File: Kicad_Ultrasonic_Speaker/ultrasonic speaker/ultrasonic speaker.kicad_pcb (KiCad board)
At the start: 2 copper layers, 99.1 x 86.4 mm, 12 parts, among them J1 To_Array, J2 Conn_01x02_Female, U1 ESP32_DevKit_V1_DOIT, U2 MIC4427, U3 LM317

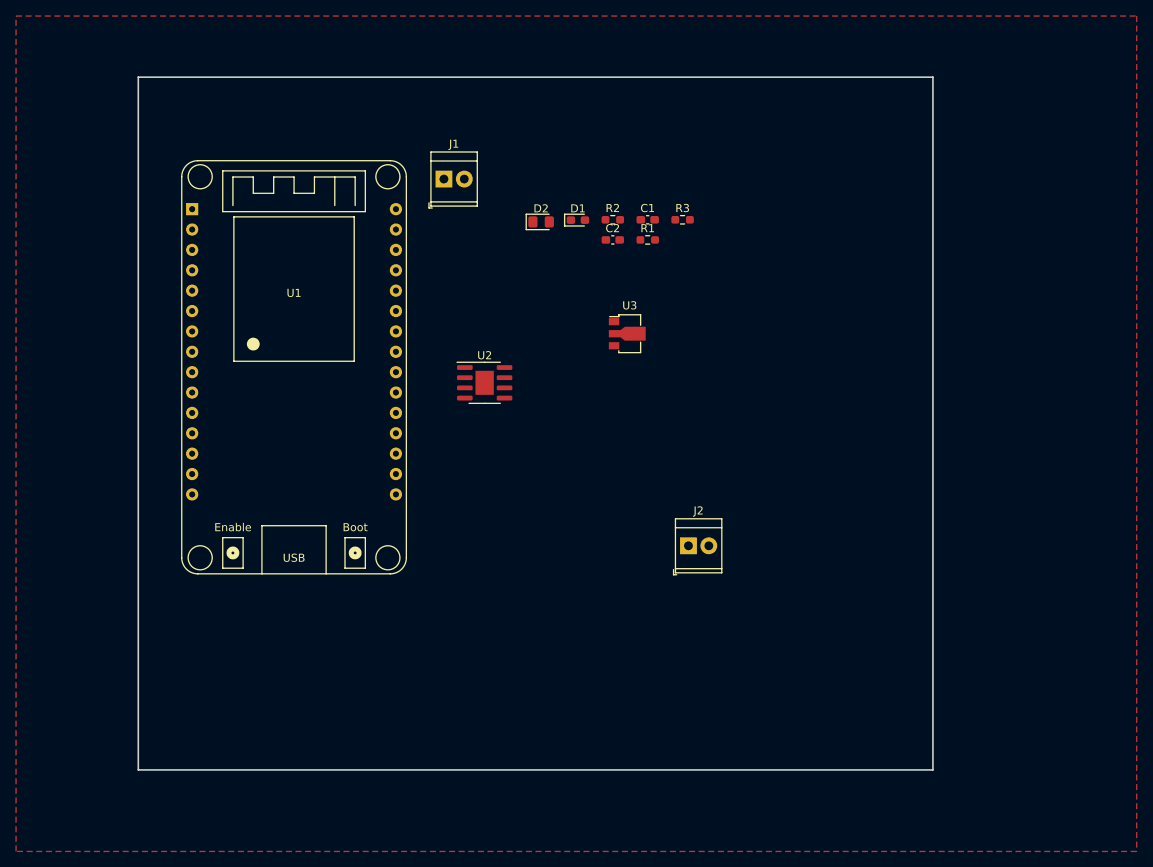
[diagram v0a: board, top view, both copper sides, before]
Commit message: change for boost converter
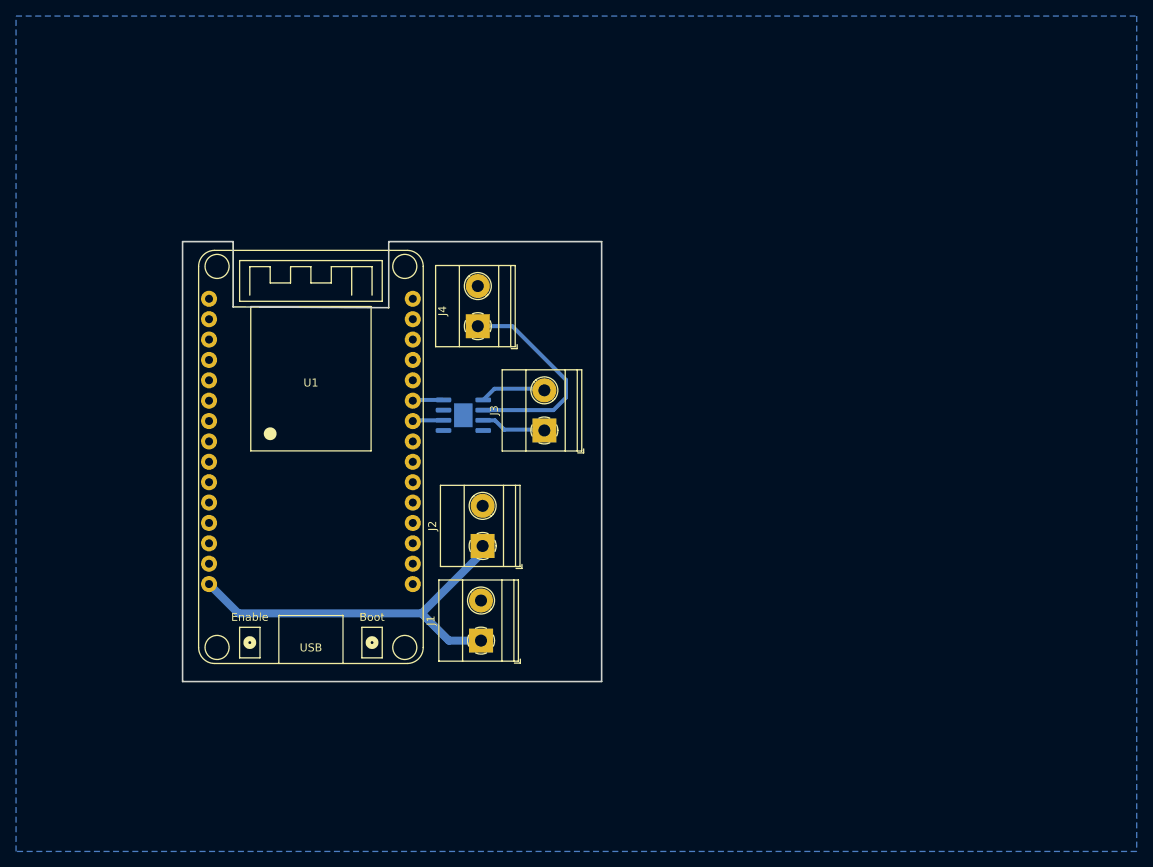
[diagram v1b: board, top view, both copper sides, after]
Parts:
- removed C1: 0.1uF, Capacitor_SMD:C_0603_1608Metric_Pad1.08x0.95mm_HandSolder
- removed C2: 1uF, Capacitor_SMD:C_0603_1608Metric_Pad1.08x0.95mm_HandSolder
- removed D1: D, Diode_SMD:D_0603_1608Metric_Pad1.05x0.95mm_HandSolder
- removed D2: LED, LED_SMD:LED_0805_2012Metric_Pad1.15x1.40mm_HandSolder
- removed R1: 390 ohm, Resistor_SMD:R_0603_1608Metric_Pad0.98x0.95mm_HandSolder
- removed R2: 240 ohm, Resistor_SMD:R_0603_1608Metric_Pad0.98x0.95mm_HandSolder
- removed R3: 1 kohm, Resistor_SMD:R_0603_1608Metric_Pad0.98x0.95mm_HandSolder
- removed U3: LM317, librarie:SOT-89-3-lm317
- added J3: To_Array, librarie:TerminalBlock_Phoenix_MKDS-1,5-2_1x02_P5.00mm_Horizontal, F.Cu at (157.3, 89.8)
- added J4: from_boost_converter, librarie:TerminalBlock_Phoenix_MKDS-1,5-2_1x02_P5.00mm_Horizontal, F.Cu at (149.0, 76.8)
- J1: value To_Array -> power supply; footprint TerminalBlock_TE-Connectivity:TerminalBlock_TE_282834-2_1x02_P2.54mm_Horizontal -> librarie:TerminalBlock_Phoenix_MKDS-1,5-2_1x02_P5.00mm_Horizontal
- J2: value Conn_01x02_Female -> to_boost_converter; footprint TerminalBlock_TE-Connectivity:TerminalBlock_TE_282834-2_1x02_P2.54mm_Horizontal -> librarie:TerminalBlock_Phoenix_MKDS-1,5-2_1x02_P5.00mm_Horizontal
- U2: moved to B.Cu
- moved J1 57.7 mm to (149.4, 116.0), turned to 90 degrees
- moved J2 25.7 mm to (149.6, 104.2), turned to 90 degrees
- moved U1 11.4 mm to (128.2, 73.3)
- moved U2 4.84 mm to (147.2, 87.9)
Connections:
- net Net-(U1-Pad24) renamed /pwm1
- net Net-(U1-Pad25) renamed /pwm2
- J1 pad 1: Net-(J1-Pad1) -> +12V
- J1 pad 2: Net-(J1-Pad2) -> GND
- J2 pad 1: VCC -> +12V
- U1 pad 15: unconnected-(U1-Pad15) -> +12V
- U1 pad 16: +3.3V -> unconnected-(U1-Pad16)
- U2 pad 5: Net-(J1-Pad2) -> Net-(J3-Pad2)
- U2 pad 6: VCC -> +24V
- U2 pad 7: Net-(J1-Pad1) -> Net-(J3-Pad1)
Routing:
- net +12V: track 0.00 -> 48.4 mm
- net +24V: track 0.00 -> 26.9 mm
- net Net-(J3-Pad2): track 0.00 -> 8.29 mm
- net Net-(J3-Pad1): track 0.00 -> 8.15 mm
- net /pwm2: track 0.00 -> 3.86 mm
- net /pwm1: track 0.00 -> 3.86 mm
- added copper zone on B.Cu, net GND
- removed copper zone on F.Cu, net GND
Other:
- board size 99.1 x 86.4 mm -> 52.2 x 54.8 mm

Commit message: modification of esp32 pcb
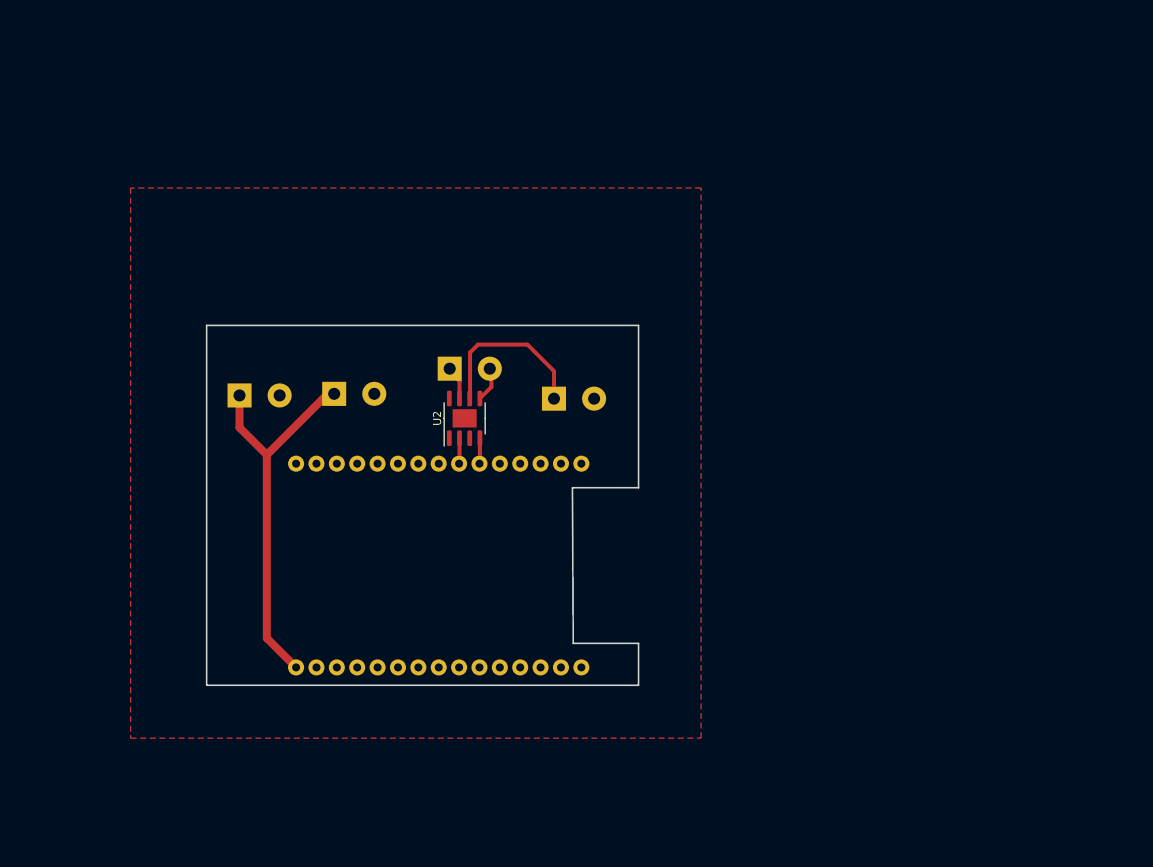
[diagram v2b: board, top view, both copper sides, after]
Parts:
- J1, J2, J3, J4, U1: moved to B.Cu
- U2: moved to F.Cu
- moved U1 47.3 mm to (161.9, 106.6), turned to 90 degrees
- moved J1 42.9 mm to (119.3, 85.4), turned to 0 degrees
- moved J2 26.5 mm to (131.1, 85.2), turned to 0 degrees
- moved J3 14.1 mm to (145.5, 82.1), turned to 0 degrees
- moved J4 13.1 mm to (158.5, 85.8), turned to 0 degrees
- moved U2 0.42 mm to (147.4, 88.2), turned to 90 degrees
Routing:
- net +24V: track 26.9 -> 21.4 mm
- net Net-(J3-Pad1): track 8.15 -> 4.22 mm
- net Net-(J3-Pad2): track 8.29 -> 4.39 mm
- net /pwm2: track 3.86 -> 3.20 mm
- net /pwm1: track 3.86 -> 3.20 mm
- added copper zone on F.Cu, net GND
- removed copper zone on B.Cu, net GND
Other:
- board size 52.2 x 54.8 mm -> 53.8 x 44.9 mm
